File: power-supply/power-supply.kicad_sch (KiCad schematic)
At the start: 22 parts, among them J1 Screw_Terminal_01x02, J2 Conn_01x03, J3 Conn_01x03, J4 Conn_01x03, J5 Conn_01x03, J6 Conn_01x03, J7 Conn_01x03, U1 L7815, U2 L7915

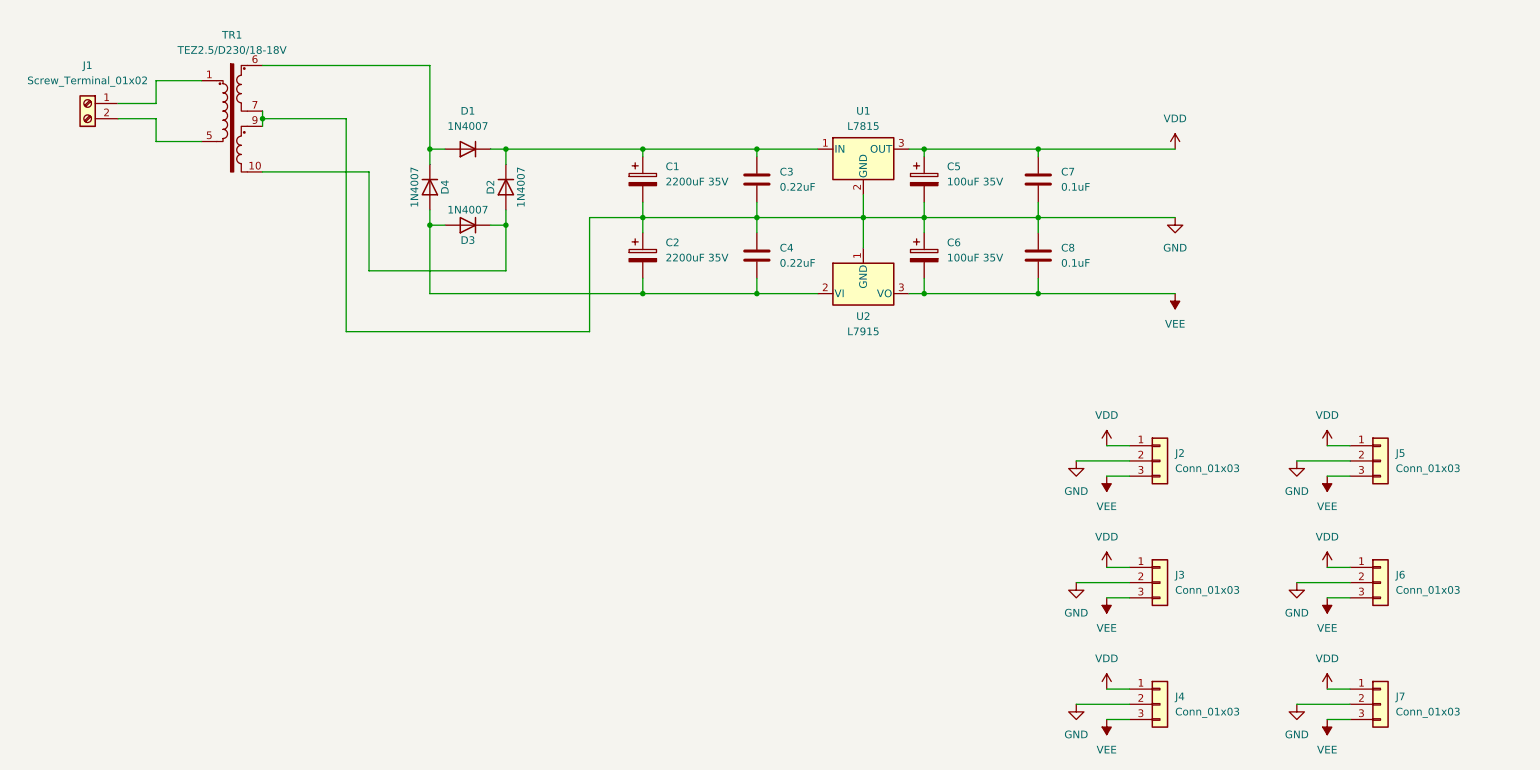
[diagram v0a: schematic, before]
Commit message: power-supply: Improved version
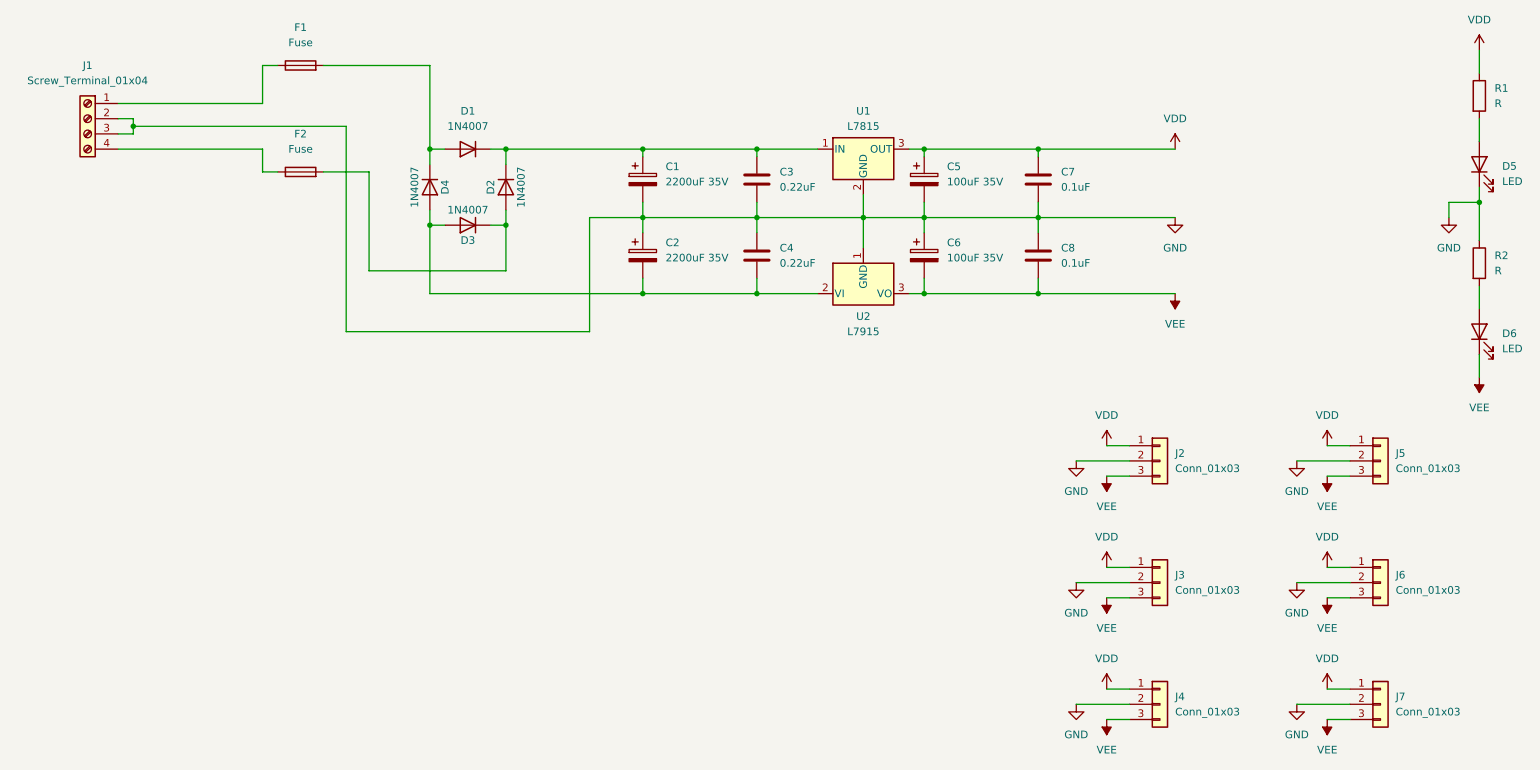
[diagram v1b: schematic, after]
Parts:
- removed TR1: TEZ2.5/D230/18-18V, Transformer_THT:Transformer_Breve_TEZ-28x33, symbol Transformer:TEZ2.5-D-2
- added D5, D6: LED, LED_THT:LED_D5.0mm, symbol Device:LED
- added F1, F2: Fuse, Resistor_THT:R_Axial_DIN0207_L6.3mm_D2.5mm_P10.16mm_Horizontal, symbol Device:Fuse
- added R1, R2: R, Resistor_THT:R_Axial_DIN0207_L6.3mm_D2.5mm_P10.16mm_Horizontal, symbol Device:R
- J1: value Screw_Terminal_01x02 -> Screw_Terminal_01x04; footprint TerminalBlock:TerminalBlock_MaiXu_MX126-5.0-02P_1x02_P5.00mm -> TerminalBlock:TerminalBlock_MaiXu_MX126-5.0-04P_1x04_P5.00mm; symbol Connector:Screw_Terminal_01x02 -> Connector:Screw_Terminal_01x04
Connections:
- net GND: now also J1.2 (Pin_2), J1.3 (Pin_3), D5.1 (K), R2.1
- net VDD: now also R1.1
- net VEE: now also D6.1 (K)
- net at D1.2 (A), D4.1 (K): now also F1.2
- net at J1.1 (Pin_1): now also F1.1
- net at D2.2 (A), D3.1 (K): now also F2.2
- new net: D5.2 (A), R1.2
- new net: D6.2 (A), R2.2
- new net: F2.1, J1.4 (Pin_4)
